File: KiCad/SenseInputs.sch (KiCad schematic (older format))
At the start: 58 parts, among them J401 TE_Connectivity_1-282834-0, J402 TE_Connectivity_282834-6, U401 ADS1115IDGST, U402 ADS1115IDGST

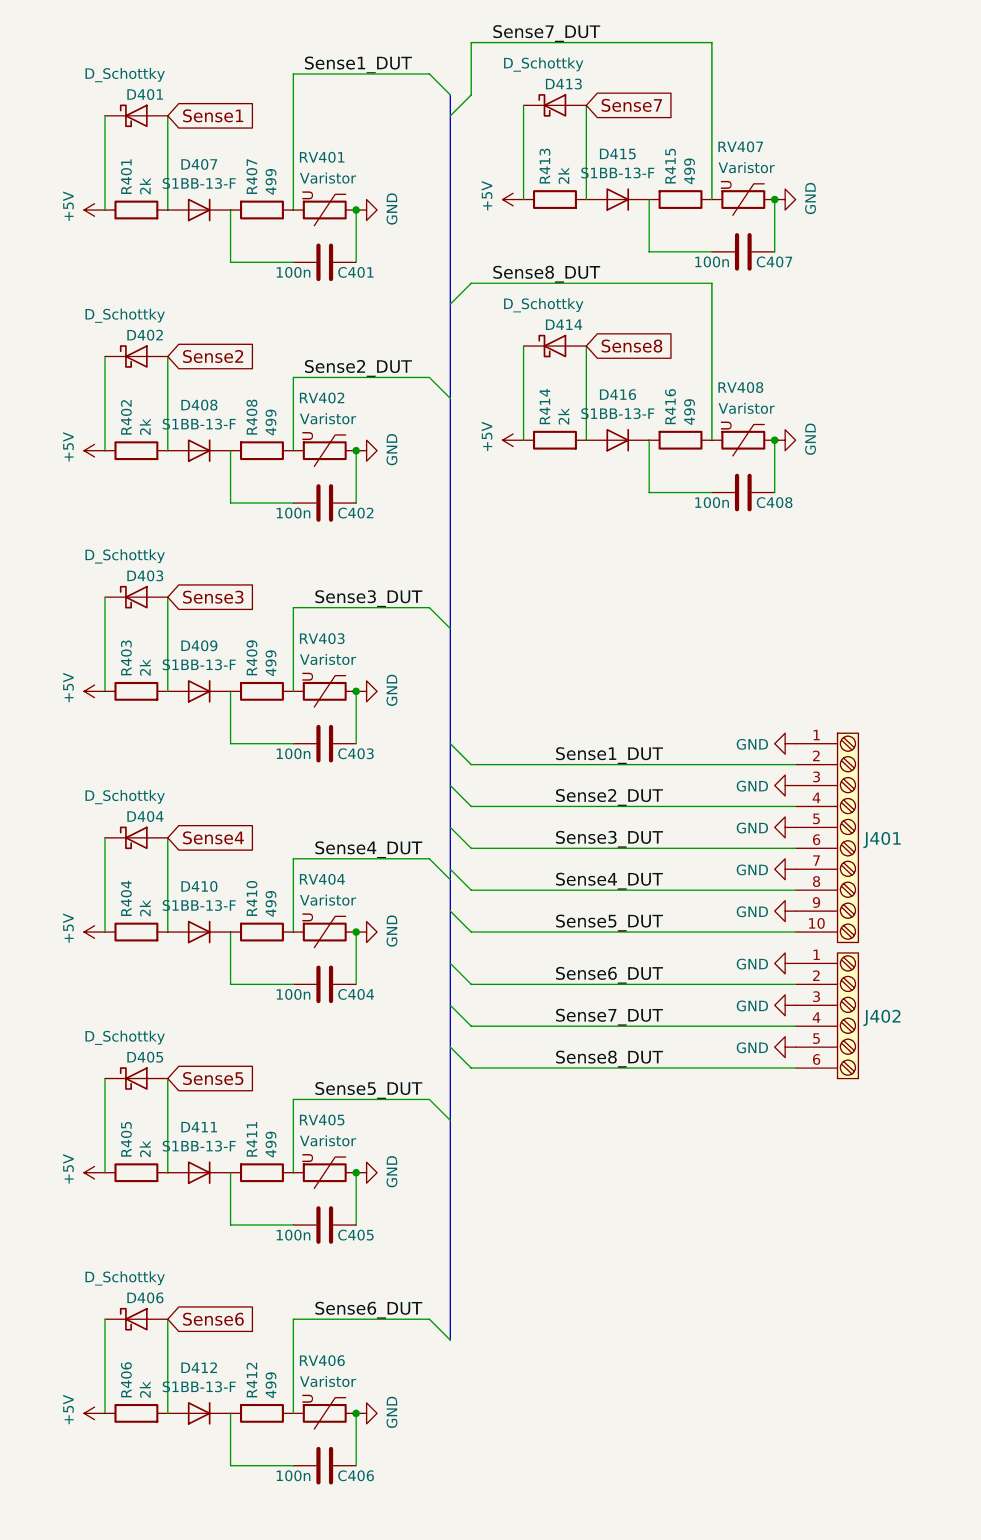
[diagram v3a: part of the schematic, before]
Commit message: New sense input circuits. New layout
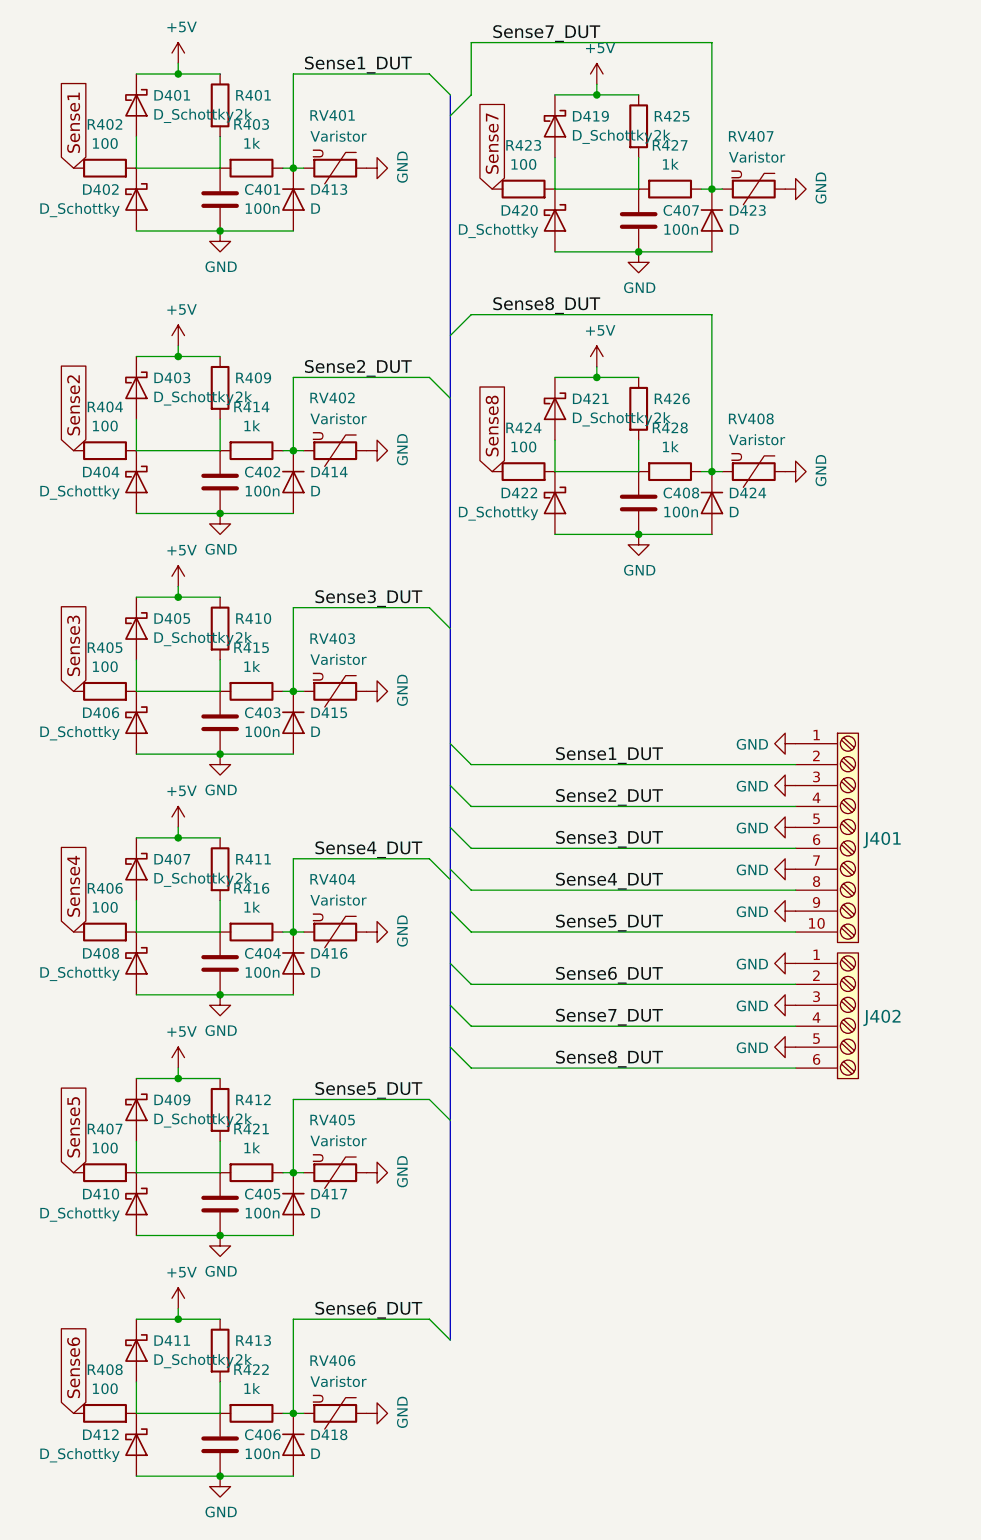
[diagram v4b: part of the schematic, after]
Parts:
- removed D407, D408, D409, D410, D411, D412, D415, D416: S1BB-13-F, Diodes_SMD:D_SMB, symbol 1N4007
- removed D413, D414: D_Schottky, Diodes_SMD:D_SOD-123, symbol D_Schottky
- added D407, D408, D409, D410, D411, D412, D419, D420, D421, D422: D_Schottky, Diodes_SMD:D_SOD-123, symbol D_Schottky
- added D413, D414, D415, D416, D417, D418, D423, D424: D, Diodes_SMD:D_SMA, symbol D
- added R421, R422, R427, R428: 1k, Resistors_SMD:R_0805, symbol R
- added R423, R424: 100, Resistors_SMD:R_0805, symbol R
- added R425, R426: 2k, Resistors_SMD:R_0805, symbol R
- R402, R404, R405, R406: value 2k -> 100
- R403, R414: value 2k -> 1k
- R407, R408: value 499 -> 100
- R409, R410, R411, R412: value 499 -> 2k
- R415, R416: value 499 -> 1k
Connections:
- net +5V: now also R409.1, R410.1, R411.1, R412.1, D407.1 (K), D409.1 (K), D411.1 (K), D419.1 (K), D421.1 (K), R425.1, R426.1; no longer D402.1 (K), D404.1 (K), D406.1 (K), R402.1, R403.1, R404.1, R405.1, R406.1, R414.1
- net GND: now also C401.1, C402.1, C403.1, C404.1, C405.1, C406.1, C407.1, C408.1, D402.2 (A), D404.2 (A), D406.2 (A), D408.2 (A), D410.2 (A), D412.2 (A), D413.2 (A), D414.2 (A), D415.2 (A), D416.2 (A), D417.2 (A), D418.2 (A), D420.2 (A), D422.2 (A), D423.2 (A), D424.2 (A); no longer C401.2, C402.2, C403.2, C404.2, C405.2, C406.2, C407.2, C408.2
- net Sense1: now also R402.1; no longer D401.2 (A), R401.2
- net Sense1_DUT: now also R403.1, D413.1 (K); no longer R407.1
- net Sense2: now also R404.1; no longer D402.2 (A), R402.2
- net Sense2_DUT: now also R414.1, D414.1 (K); no longer R408.1
- net Sense3: now also R405.1; no longer D403.2 (A), R403.2
- net Sense3_DUT: now also R415.1, D415.1 (K); no longer R409.1
- net Sense4: now also R406.1; no longer D404.2 (A), R404.2
- net Sense4_DUT: now also R416.1, D416.1 (K); no longer R410.1
- net Sense5: now also R407.1; no longer D405.2 (A), R405.2
- net Sense5_DUT: now also D417.1 (K), R421.1; no longer R411.1
- net Sense6: now also R408.1; no longer D406.2 (A), R406.2
- net Sense6_DUT: now also D418.1 (K), R422.1; no longer R412.1
- net Sense7: now also R423.1; no longer R413.2
- net Sense7_DUT: now also D423.1 (K), R427.1; no longer R415.1
- net Sense8: now also R424.1; no longer R414.2
- net Sense8_DUT: now also D424.1 (K), R428.1; no longer R416.1
- net at R407.2: now also C405.2, R412.2, D409.2 (A), D410.1 (K), R421.2; no longer C401.1
- net at R408.2: now also C406.2, R413.2, D411.2 (A), D412.1 (K), R422.2; no longer C402.1
- net at R409.2: now also C402.2, D403.2 (A), D404.1 (K), R404.2, R414.2; no longer C403.1
- net at R410.2: now also C403.2, D405.2 (A), D406.1 (K), R405.2, R415.2; no longer C404.1
- net at R411.2: now also C404.2, R406.2, R416.2, D407.2 (A), D408.1 (K); no longer C405.1
- new net: C401.2, D401.2 (A), D402.1 (K), R401.2, R402.2, R403.2
- new net: C407.2, D419.2 (A), D420.1 (K), R423.2, R425.2, R427.2
- new net: C408.2, D421.2 (A), D422.1 (K), R424.2, R426.2, R428.2
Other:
- moved on the sheet: C401, R401, RV401
